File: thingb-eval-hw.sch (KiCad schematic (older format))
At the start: 37 parts, among them J1 USB_C_Receptacle_USB2.0, J2 Conn_01x04, J3 Conn_01x04, Q1 S9015, SW1 SW_Push, SW2 SW_Push, SW3 TSWB-3N-CB, U1 ESP32-WROVER, U2 MCP23008_SO, U3 XC6222B281MR-G, U4 NVT2008, U5 ER-TFT1.44-1, U6 L80-R

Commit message: associate footprints with all parts
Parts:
- BT1: footprint (none) -> Connector_PinHeader_2.54mm:PinHeader_1x02_P2.54mm_Vertical
- C1, C10, C11, C2, C3, C4, C5, C6, C7, C8, C9: footprint (none) -> Capacitor_SMD:C_0603_1608Metric_Pad1.05x0.95mm_HandSolder
- J1: footprint (none) -> thingb:U262-16XN-4BVC11
- J2, J3: footprint (none) -> Connector_PinHeader_2.54mm:PinHeader_1x04_P2.54mm_Vertical
- Q1: footprint (none) -> Package_TO_SOT_SMD:SOT-23_Handsoldering
- R1, R10, R11, R12, R2, R3, R4, R5, R6, R7, R8, R9: footprint (none) -> Resistor_SMD:R_0603_1608Metric_Pad1.05x0.95mm_HandSolder
- SW1, SW2: footprint (none) -> Button_Switch_THT:SW_PUSH_6mm_H5mm
- SW3: footprint (none) -> thingb:TSWB-3N-CB
- U1: footprint RF_Module:ESP32-WROVER -> thingb:ESP32-WROVER
- U4: footprint (none) -> Package_SO:TSSOP-20_4.4x6.5mm_P0.65mm
- U5: footprint (none) -> thingb:ER-TFT1.44-1
- U6: footprint (none) -> thingb:L80-R
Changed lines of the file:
@@
 F 0 "R3" H 2468 2246 50  0000 L CNN
 F 1 "5.1k" H 2468 2155 50  0000 L CNN
-F 2 "" H 2400 2200 50  0001 C CNN
+F 2 "Resistor_SMD:R_0603_1608Metric_Pad1.05x0.95mm_HandSolder" H 2400 2200 50  0001 C CNN
 F 3 "~" H 2400 2200 50  0001 C CNN
 	1    2400 2200
@@
 F 0 "R2" H 2118 2296 50  0000 L CNN
 F 1 "5.1k" H 2118 2205 50  0000 L CNN
-F 2 "" H 2050 2250 50  0001 C CNN
+F 2 "Resistor_SMD:R_0603_1608Metric_Pad1.05x0.95mm_HandSolder" H 2050 2250 50  0001 C CNN
 F 3 "~" H 2050 2250 50  0001 C CNN
 	1    2050 2250
@@
 F 0 "J1" H 1057 3267 50  0000 C CNN
 F 1 "USB_C_Receptacle_USB2.0" H 1057 3176 50  0000 C CNN
-F 2 "" H 1100 2400 50  0001 C CNN
+F 2 "thingb:U262-16XN-4BVC11" H 1100 2400 50  0001 C CNN
 F 3 "https://www.usb.org/sites/default/files/documents/usb_type-c.zip" H 1100 2400 50  0001 C CNN
 	1    950  2400
@@
 F 0 "BT1" H 2418 1246 50  0000 L CNN
 F 1 "Battery_Cell" H 2418 1155 50  0000 L CNN
-F 2 "" V 2300 1210 50  0001 C CNN
+F 2 "Connector_PinHeader_2.54mm:PinHeader_1x02_P2.54mm_Vertical" V 2300 1210 50  0001 C CNN
 F 3 "~" V 2300 1210 50  0001 C CNN
 	1    2300 1150
@@
 F 0 "C4" H 5292 1446 50  0000 L CNN
 F 1 "1uF" H 5292 1355 50  0000 L CNN
-F 2 "" H 5200 1400 50  0001 C CNN
+F 2 "Capacitor_SMD:C_0603_1608Metric_Pad1.05x0.95mm_HandSolder" H 5200 1400 50  0001 C CNN
 F 3 "~" H 5200 1400 50  0001 C CNN
 	1    5200 1400
@@
 F 0 "C6" H 6392 1446 50  0000 L CNN
 F 1 "4.7uF" H 6392 1355 50  0000 L CNN
-F 2 "" H 6300 1400 50  0001 C CNN
+F 2 "Capacitor_SMD:C_0603_1608Metric_Pad1.05x0.95mm_HandSolder" H 6300 1400 50  0001 C CNN
 F 3 "~" H 6300 1400 50  0001 C CNN
 	1    6300 1400
@@
 F 0 "R1" H 1218 4146 50  0000 L CNN
 F 1 "10k" H 1218 4055 50  0000 L CNN
-F 2 "" H 1150 4100 50  0001 C CNN
+F 2 "Resistor_SMD:R_0603_1608Metric_Pad1.05x0.95mm_HandSolder" H 1150 4100 50  0001 C CNN
 F 3 "~" H 1150 4100 50  0001 C CNN
 	1    1150 4100
@@
 F 0 "SW1" H 850 4575 50  0000 C CNN
 F 1 "SW_Push" H 850 4484 50  0000 C CNN
-F 2 "" H 850 4250 50  0001 C CNN
+F 2 "Button_Switch_THT:SW_PUSH_6mm_H5mm" H 850 4250 50  0001 C CNN
 F 3 "~" H 850 4250 50  0001 C CNN
 	1    850  4250
@@
 F 0 "C1" H 2292 4146 50  0000 L CNN
 F 1 "22uF" H 2292 4055 50  0000 L CNN
-F 2 "" H 2200 4100 50  0001 C CNN
+F 2 "Capacitor_SMD:C_0603_1608Metric_Pad1.05x0.95mm_HandSolder" H 2200 4100 50  0001 C CNN
 F 3 "~" H 2200 4100 50  0001 C CNN
 	1    2200 4100
@@
 F 0 "C2" H 2692 4146 50  0000 L CNN
 F 1 "0.1uF" H 2692 4055 50  0000 L CNN
-F 2 "" H 2600 4100 50  0001 C CNN
+F 2 "Capacitor_SMD:C_0603_1608Metric_Pad1.05x0.95mm_HandSolder" H 2600 4100 50  0001 C CNN
 F 3 "~" H 2600 4100 50  0001 C CNN
 	1    2600 4100
@@
 F 0 "SW2" H 2900 4925 50  0000 C CNN
 F 1 "SW_Push" H 2900 4834 50  0000 C CNN
-F 2 "" H 2900 4600 50  0001 C CNN
+F 2 "Button_Switch_THT:SW_PUSH_6mm_H5mm" H 2900 4600 50  0001 C CNN
 F 3 "~" H 2900 4600 50  0001 C CNN
 	1    2900 4600
@@
 F 0 "U6" H 8457 2688 39  0000 R CNN
 F 1 "L80-R" H 8457 2613 39  0000 R CNN
-F 2 "" H 9050 2650 39  0001 C CNN
+F 2 "thingb:L80-R" H 9050 2650 39  0001 C CNN
 F 3 "https://www.quectel.com/UploadImage/Downlad/Quectel_L80-R_Hardware_Design_V1.2.pdf" H 9050 2650 39  0001 C CNN
 	1    9050 2650
@@
 F 0 "C9" H 9492 1996 50  0000 L CNN
 F 1 "10uF" H 9492 1905 50  0000 L CNN
-F 2 "" H 9400 1950 50  0001 C CNN
+F 2 "Capacitor_SMD:C_0603_1608Metric_Pad1.05x0.95mm_HandSolder" H 9400 1950 50  0001 C CNN
 F 3 "~" H 9400 1950 50  0001 C CNN
 	1    9400 1950
@@
 F 0 "C10" H 9892 1996 50  0000 L CNN
 F 1 "0.1uF" H 9892 1905 50  0000 L CNN
-F 2 "" H 9800 1950 50  0001 C CNN
+F 2 "Capacitor_SMD:C_0603_1608Metric_Pad1.05x0.95mm_HandSolder" H 9800 1950 50  0001 C CNN
 F 3 "~" H 9800 1950 50  0001 C CNN
 	1    9800 1950
@@
 F 0 "C11" H 10292 1996 50  0000 L CNN
 F 1 "0.1uF" H 10292 1905 50  0000 L CNN
-F 2 "" H 10200 1950 50  0001 C CNN
+F 2 "Capacitor_SMD:C_0603_1608Metric_Pad1.05x0.95mm_HandSolder" H 10200 1950 50  0001 C CNN
 F 3 "~" H 10200 1950 50  0001 C CNN
 	1    10200 1950
@@
 F 0 "R10" H 8282 2404 50  0000 R CNN
 F 1 "10k" H 8282 2495 50  0000 R CNN
-F 2 "" H 8350 2450 50  0001 C CNN
+F 2 "Resistor_SMD:R_0603_1608Metric_Pad1.05x0.95mm_HandSolder" H 8350 2450 50  0001 C CNN
 F 3 "~" H 8350 2450 50  0001 C CNN
 	1    8350 2450
@@
 F 0 "U5" H 8800 6528 50  0000 C CNN
 F 1 "ER-TFT1.44-1" H 8800 6437 50  0000 C CNN
-F 2 "" H 8800 5600 50  0001 C CNN
+F 2 "thingb:ER-TFT1.44-1" H 8800 5600 50  0001 C CNN
 F 3 "" H 8800 5600 50  0001 C CNN
 	1    8800 5600
@@
 F 0 "R9" H 7632 5454 50  0000 R CNN
 F 1 "10k" H 7632 5545 50  0000 R CNN
-F 2 "" H 7700 5500 50  0001 C CNN
+F 2 "Resistor_SMD:R_0603_1608Metric_Pad1.05x0.95mm_HandSolder" H 7700 5500 50  0001 C CNN
 F 3 "~" H 7700 5500 50  0001 C CNN
 	1    7700 5500
@@
 F 0 "C8" H 9292 4546 50  0000 L CNN
 F 1 "0.1uF" H 9292 4455 50  0000 L CNN
-F 2 "" H 9200 4500 50  0001 C CNN
+F 2 "Capacitor_SMD:C_0603_1608Metric_Pad1.05x0.95mm_HandSolder" H 9200 4500 50  0001 C CNN
 F 3 "~" H 9200 4500 50  0001 C CNN
 	1    9200 4500
@@
 F 0 "R11" V 9700 5300 50  0000 C CNN
 F 1 "R_Small_US" V 9800 5300 50  0000 C CNN
-F 2 "" H 9600 5300 50  0001 C CNN
+F 2 "Resistor_SMD:R_0603_1608Metric_Pad1.05x0.95mm_HandSolder" H 9600 5300 50  0001 C CNN
 F 3 "~" H 9600 5300 50  0001 C CNN
 	1    9600 5300
@@
 F 0 "U4" H 6250 4415 50  0000 C CNN
 F 1 "NVT2008" H 6250 4324 50  0000 C CNN
-F 2 "" H 6250 3650 50  0001 C CNN
+F 2 "Package_SO:TSSOP-20_4.4x6.5mm_P0.65mm" H 6250 3650 50  0001 C CNN
 F 3 "" H 6250 3650 50  0001 C CNN
 	1    6250 3650
@@
 F 0 "SW3" H 4600 8015 50  0000 C CNN
 F 1 "TSWB-3N-CB" H 4600 7924 50  0000 C CNN
-F 2 "" H 4600 7450 50  0001 C CNN
+F 2 "thingb:TSWB-3N-CB" H 4600 7450 50  0001 C CNN
 F 3 "" H 4600 7450 50  0001 C CNN
 	1    4600 7450
@@
 F 0 "U1" H 1400 7150 50  0000 C CNN
 F 1 "ESP32-WROVER" H 2200 7150 50  0000 C CNN
-F 2 "RF_Module:ESP32-WROVER" H 1850 4300 50  0001 C CNN
+F 2 "thingb:ESP32-WROVER" H 1850 4300 50  0001 C CNN
 F 3 "https://www.espressif.com/sites/default/files/documentation/esp32-wroom-32_datasheet_en.pdf" H 1550 5850 50  0001 C CNN
 	1    1850 5800
@@
 F 0 "R5" H 5318 3296 50  0000 L CNN
 F 1 "10k" H 5318 3205 50  0000 L CNN
-F 2 "" H 5250 3250 50  0001 C CNN
+F 2 "Resistor_SMD:R_0603_1608Metric_Pad1.05x0.95mm_HandSolder" H 5250 3250 50  0001 C CNN
 F 3 "~" H 5250 3250 50  0001 C CNN
 	1    5250 3250
@@
 F 0 "R6" H 7168 3396 50  0000 L CNN
 F 1 "10k" H 7168 3305 50  0000 L CNN
-F 2 "" H 7100 3350 50  0001 C CNN
+F 2 "Resistor_SMD:R_0603_1608Metric_Pad1.05x0.95mm_HandSolder" H 7100 3350 50  0001 C CNN
 F 3 "~" H 7100 3350 50  0001 C CNN
 	1    7100 3350
@@
 F 0 "R7" H 7168 4096 50  0000 L CNN
 F 1 "10k" H 7168 4005 50  0000 L CNN
-F 2 "" H 7100 4050 50  0001 C CNN
+F 2 "Resistor_SMD:R_0603_1608Metric_Pad1.05x0.95mm_HandSolder" H 7100 4050 50  0001 C CNN
 F 3 "~" H 7100 4050 50  0001 C CNN
 	1    7100 4050
@@
 F 0 "R8" H 7518 4096 50  0000 L CNN
 F 1 "10k" H 7518 4005 50  0000 L CNN
-F 2 "" H 7450 4050 50  0001 C CNN
+F 2 "Resistor_SMD:R_0603_1608Metric_Pad1.05x0.95mm_HandSolder" H 7450 4050 50  0001 C CNN
 F 3 "~" H 7450 4050 50  0001 C CNN
 	1    7450 4050
@@
 F 0 "R4" H 4868 3696 50  0000 L CNN
 F 1 "10k" H 4868 3605 50  0000 L CNN
-F 2 "" H 4800 3650 50  0001 C CNN
+F 2 "Resistor_SMD:R_0603_1608Metric_Pad1.05x0.95mm_HandSolder" H 4800 3650 50  0001 C CNN
 F 3 "~" H 4800 3650 50  0001 C CNN
 	1    4800 3650
@@
 F 0 "J3" H 7868 1367 50  0000 C CNN
 F 1 "Conn_01x04" H 7868 1276 50  0000 C CNN
-F 2 "" H 7950 1050 50  0001 C CNN
+F 2 "Connector_PinHeader_2.54mm:PinHeader_1x04_P2.54mm_Vertical" H 7950 1050 50  0001 C CNN
 F 3 "~" H 7950 1050 50  0001 C CNN
 	1    7950 1050
@@
 F 0 "C3" H 5092 4946 50  0000 L CNN
 F 1 "0.1uF" H 5092 4855 50  0000 L CNN
-F 2 "" H 5000 4900 50  0001 C CNN
+F 2 "Capacitor_SMD:C_0603_1608Metric_Pad1.05x0.95mm_HandSolder" H 5000 4900 50  0001 C CNN
 F 3 "~" H 5000 4900 50  0001 C CNN
 	1    5000 4900
@@
 F 0 "C5" H 5792 2846 50  0000 L CNN
 F 1 "0.1uF" H 5792 2755 50  0000 L CNN
-F 2 "" H 5700 2800 50  0001 C CNN
+F 2 "Capacitor_SMD:C_0603_1608Metric_Pad1.05x0.95mm_HandSolder" H 5700 2800 50  0001 C CNN
 F 3 "~" H 5700 2800 50  0001 C CNN
 	1    5700 2800
@@
 F 0 "C7" H 6892 2846 50  0000 L CNN
 F 1 "0.1uF" H 6892 2755 50  0000 L CNN
-F 2 "" H 6800 2800 50  0001 C CNN
+F 2 "Capacitor_SMD:C_0603_1608Metric_Pad1.05x0.95mm_HandSolder" H 6800 2800 50  0001 C CNN
 F 3 "~" H 6800 2800 50  0001 C CNN
 	1    6800 2800
@@
 F 0 "J2" H 3918 4067 50  0000 C CNN
 F 1 "Conn_01x04" H 3918 3976 50  0000 C CNN
-F 2 "" H 4000 3750 50  0001 C CNN
+F 2 "Connector_PinHeader_2.54mm:PinHeader_1x04_P2.54mm_Vertical" H 4000 3750 50  0001 C CNN
 F 3 "~" H 4000 3750 50  0001 C CNN
 	1    4000 3750
@@
 F 0 "Q1" H 10240 4854 50  0000 L CNN
 F 1 "S9015" H 10240 4945 50  0000 L CNN
-F 2 "" H 10250 5000 50  0001 C CNN
+F 2 "Package_TO_SOT_SMD:SOT-23_Handsoldering" H 10250 5000 50  0001 C CNN
 F 3 "~" H 10050 4900 50  0001 C CNN
 	1    10050 4900
@@
 F 0 "R12" V 9800 4900 50  0000 C CNN
 F 1 "1k" V 9900 4900 50  0000 C CNN
-F 2 "" H 9700 4900 50  0001 C CNN
+F 2 "Resistor_SMD:R_0603_1608Metric_Pad1.05x0.95mm_HandSolder" H 9700 4900 50  0001 C CNN
 F 3 "~" H 9700 4900 50  0001 C CNN
 	1    9700 4900

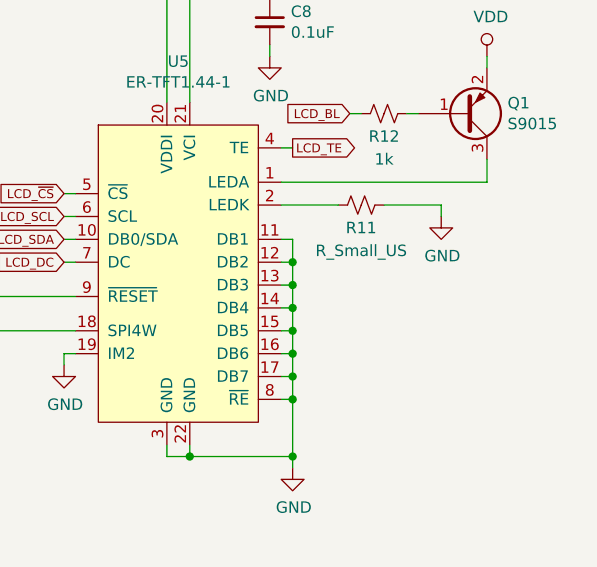
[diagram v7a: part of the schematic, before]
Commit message: replace backlight resistor with 15 mA constant-current driver, to ensure screen brightness is consistent as battery depletes
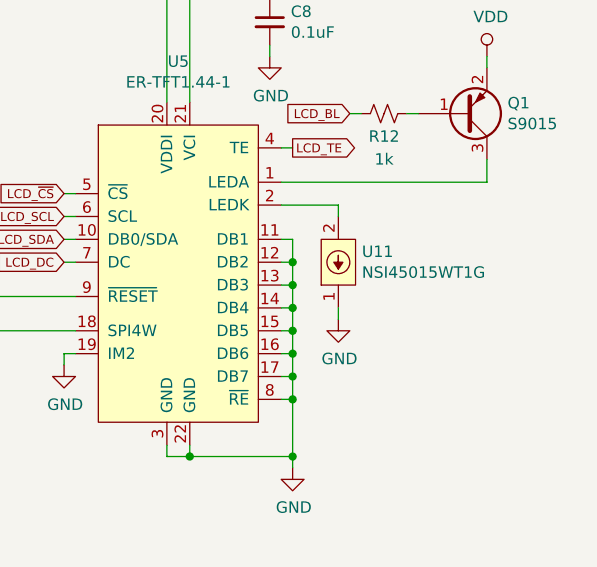
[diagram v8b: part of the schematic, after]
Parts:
- removed R11: R_Small_US, Resistor_SMD:R_0603_1608Metric_Pad1.05x0.95mm_HandSolder, symbol Device:R_Small_US
- added U11: NSI45015WT1G, Diode_SMD:D_SOD-123, symbol thingb:NSI45015WT1G
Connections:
- net GND: now also U11.1
- net at U5.2 (LEDK): now also U11.2
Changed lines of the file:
@@
 Wire Wire Line
 	8300 5250 8350 5250
-$Comp
-L Device:R_Small_US R11
-U 1 1 5CADEEFF
-P 9600 5300
-F 0 "R11" V 9700 5300 50  0000 C CNN
-F 1 "R_Small_US" V 9800 5300 50  0000 C CNN
-F 2 "Resistor_SMD:R_0603_1608Metric_Pad1.05x0.95mm_HandSolder" H 9600 5300 50  0001 C CNN
-F 3 "~" H 9600 5300 50  0001 C CNN
-	1    9600 5300
-	0    1    1    0
-$EndComp
 Wire Wire Line
 	9250 5300 9500 5300
-Wire Wire Line
-	9700 5300 9950 5300
 $Comp
 L thingb:NVT2008 U4
@@
 Wire Wire Line
 	9300 6150 9300 6400
-Wire Wire Line
-	9950 5300 9950 5350
 $Comp
 L power:GND #PWR045
 U 1 1 5D7A48D8
-P 9950 5350
-F 0 "#PWR045" H 9950 5100 50  0001 C CNN
-F 1 "GND" H 9955 5177 50  0000 C CNN
-F 2 "" H 9950 5350 50  0001 C CNN
-F 3 "" H 9950 5350 50  0001 C CNN
-	1    9950 5350
+P 9500 5800
+F 0 "#PWR045" H 9500 5550 50  0001 C CNN
+F 1 "GND" H 9505 5627 50  0000 C CNN
+F 2 "" H 9500 5800 50  0001 C CNN
+F 3 "" H 9500 5800 50  0001 C CNN
+	1    9500 5800
 	1    0    0    -1
 $EndComp
@@
 Wire Wire Line
 	9800 4900 9850 4900
+Wire Wire Line
+	9500 5300 9500 5350
+Wire Wire Line
+	9500 5800 9500 5750
+$Comp
+L thingb:NSI45015WT1G U11
+U 1 1 5DB5BF49
+P 9500 5550
+F 0 "U11" H 9603 5596 50  0000 L CNN
+F 1 "NSI45015WT1G" H 9603 5505 50  0000 L CNN
+F 2 "Diode_SMD:D_SOD-123" H 9500 5550 50  0001 C CNN
+F 3 "https://datasheet.lcsc.com/szlcsc/ON-Semicon-ON-NSI45015WT1G_C328096.pdf" H 9500 5550 50  0001 C CNN
+	1    9500 5550
+	1    0    0    -1
+$EndComp
 $EndSCHEMATC
